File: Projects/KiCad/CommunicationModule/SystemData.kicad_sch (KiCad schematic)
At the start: 23 parts, among them J1 Conn_01x04_Pin, J2 Conn_01x04_Pin, J3 Micro_SD_Card_Det_Hirose_DM3AT, U1 ABX00012, U2 MCP2562-E-P, U3 LT1584-3.3, U4 TLP222A, U5 MCP2515-I/P, Y1 8MHz

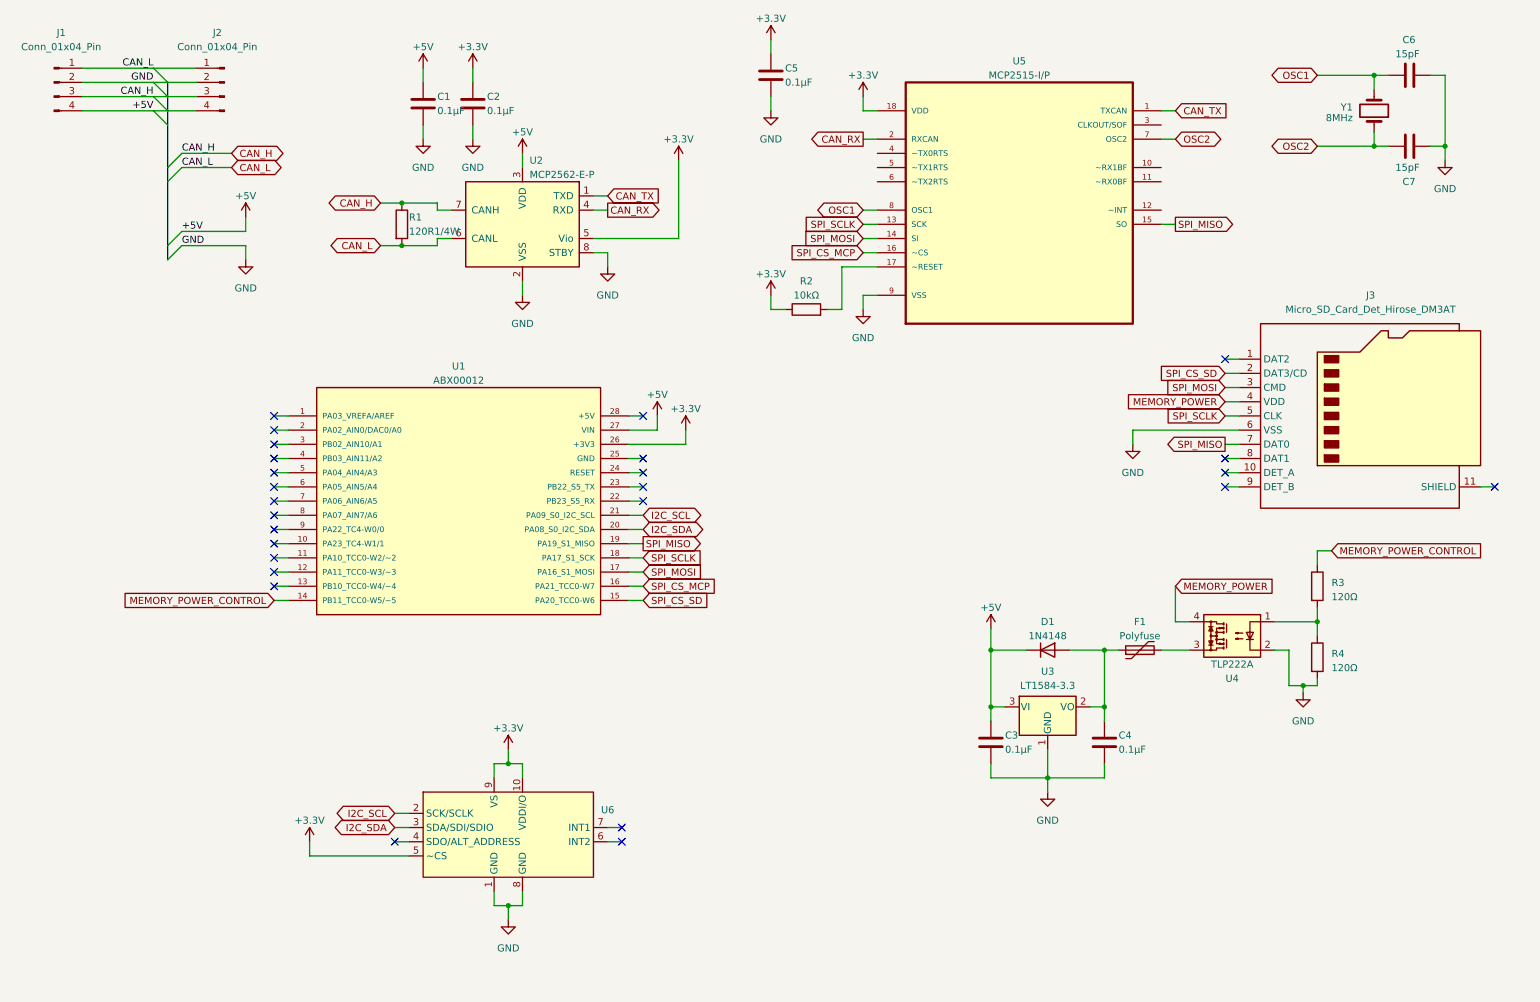
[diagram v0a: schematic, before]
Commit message: ミッションモジュール, エアデータ通信モジュール, システムデータ通信モジュールのKiCadを追加
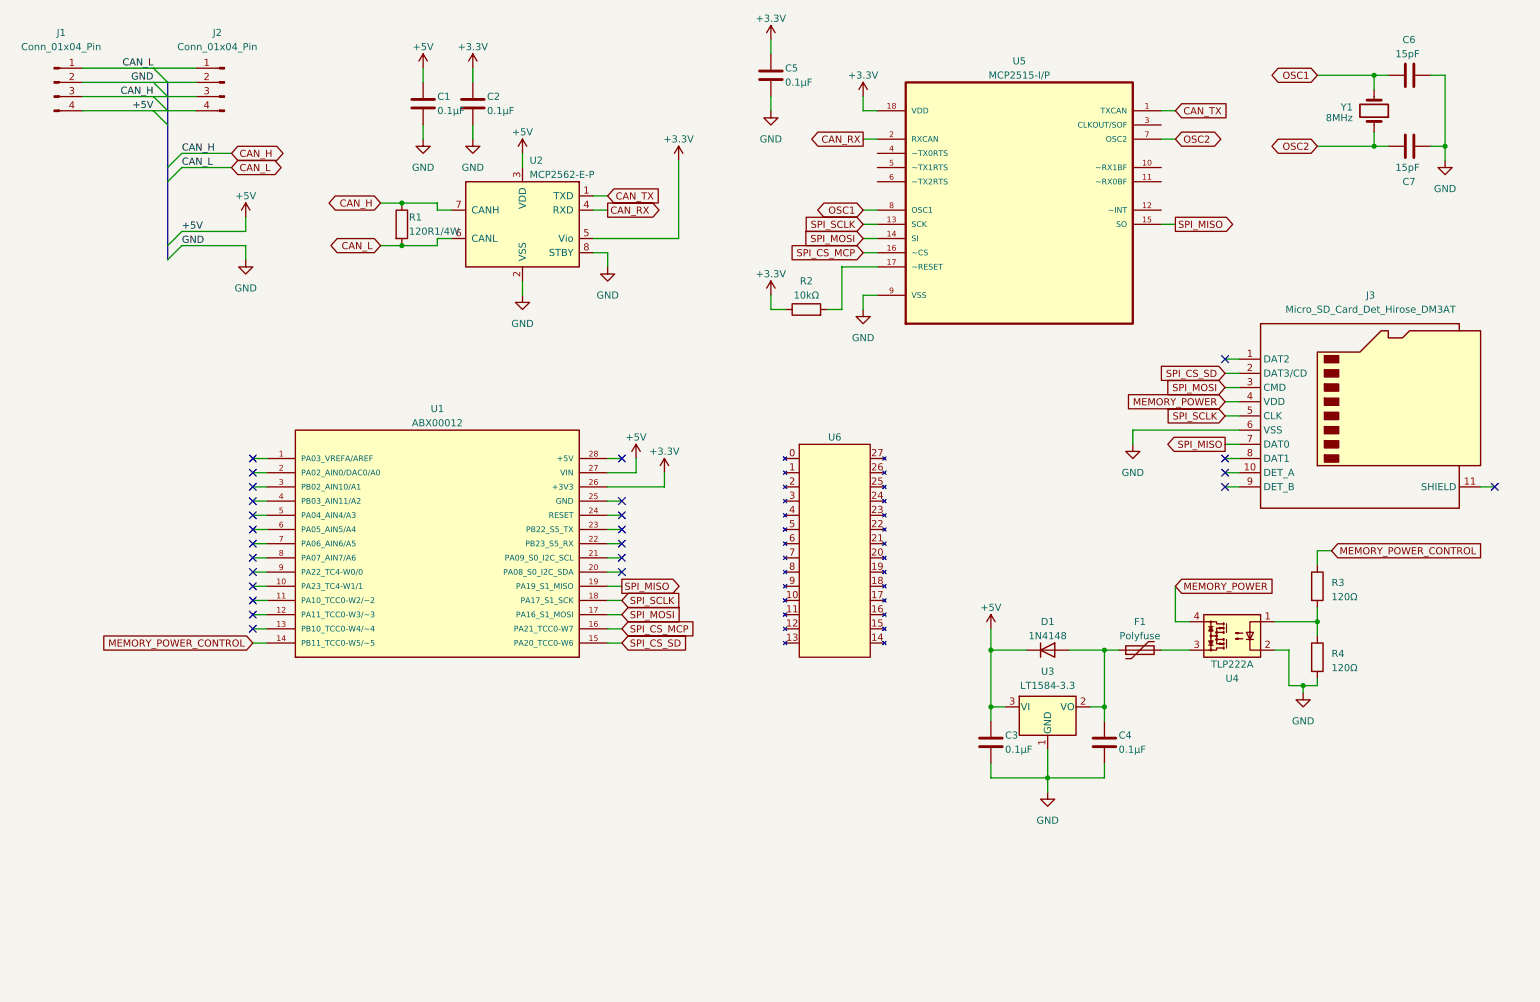
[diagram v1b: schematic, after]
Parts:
- removed U6: ~, StrawberryLinux_ADXL375_Module:ADXL375, symbol StrawberryLinux_ADXL375_Module:ADXL375
- added U6: ~, ArduinoMkrGpsShield:Arduino MKR GPS Shield, symbol ArduinoMkrGpsShield:Arduino_MKR_GPS_Shield
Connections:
- net I2C_SCL: no longer names the net of U1.21 (PA09_S0_I2C_SCL)
- net I2C_SDA: no longer names the net of U1.20 (PA08_S0_I2C_SDA)
- no-connect marks 26 -> 25
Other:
- moved on the sheet: U1

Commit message: 全モジュールのkicadを一通り作った
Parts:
- removed C3, C4: 0.1μF, Capacitor_SMD:C_0805_2012Metric_Pad1.18x1.45mm_HandSolder, symbol Device:C
- removed D1: 1N4148, Diode_THT:D_DO-35_SOD27_P7.62mm_Horizontal, symbol Diode:1N4148
- removed F1: Polyfuse, Fuse:Fuse_BelFuse_0ZRE0005FF_L8.3mm_W3.8mm, symbol Device:Polyfuse
- removed J3: Micro_SD_Card_Det_Hirose_DM3AT, Connector_Card:microSD_HC_Hirose_DM3AT-SF-PEJM5, symbol Connector:Micro_SD_Card_Det_Hirose_DM3AT
- removed U3: LT1584-3.3, Package_TO_SOT_THT:TO-220-3_Vertical, symbol Regulator_Linear:LT1584-3.3
- removed U4: TLP222A, Package_DIP:DIP-4_W7.62mm, symbol Relay_SolidState:TLP222A
- added D1, D2, D3, D4, D5, D6: LED, LED_SMD:LED_1206_3216Metric_Pad1.42x1.75mm_HandSolder, symbol Device:LED
- added R5, R6, R7, R8: 100Ω, Resistor_SMD:R_0805_2012Metric_Pad1.20x1.40mm_HandSolder, symbol Device:R
- added SW1: SW_Push, Button_Switch_THT:SW_PUSH_6mm, symbol Switch:SW_Push
- R2: footprint (none) -> Resistor_SMD:R_0805_2012Metric_Pad1.20x1.40mm_HandSolder
- R3: value 120Ω -> 2kΩ
- R4: value 120Ω -> 100Ω
- renumbered C5 to C3, C6 to C4, C7 to C5, U6 to U3, U5 to U4
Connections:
- net +5V: now also R3.1
- net GND: now also D1.1 (K), D2.1 (K), D3.1 (K), D4.1 (K), D5.1 (K), D6.1 (K), SW1.1; no longer R4.2
- net at R3.2: now also D1.2 (A); no longer R4.1
- net CAN_RECEIVE_STATUS: now reaches U1.10 (PA23_TC4-W1/1)
- net CAN_RECEIVE_STATUS: now also R4.1
- net CAN_SEND_STATUS: now reaches U1.11 (PA10_TCC0-W2/~2)
- net CAN_SEND_STATUS: now also R5.1
- net LORA_RECEIVE_STATUS: now reaches U1.12 (PA11_TCC0-W3/~3)
- net LORA_RECEIVE_STATUS: now also R6.1
- net LORA_SEND_STATUS: now reaches U1.13 (PB10_TCC0-W4/~4)
- net LORA_SEND_STATUS: now also R7.1
- net DEBUG_MODE: now reaches U1.9 (PA22_TC4-W0/0)
- net DEBUG_MODE: now also SW1.2
- net MEMORY_POWER_CONTROL renamed GNSS_STATUS
- net GNSS_STATUS: now also R8.1; no longer R3.1
- net SPI_CS_SD: no longer names the net of U1.15 (PA20_TCC0-W6)
- new net: D6.2 (A), R8.2
- new net: D2.2 (A), R4.2
- new net: D3.2 (A), R5.2
- new net: D5.2 (A), R7.2
- new net: D4.2 (A), R6.2
- no-connect marks 25 -> 16

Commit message: 一通り部品を選定
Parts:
- C4, C5: footprint Capacitor_SMD:C_0805_2012Metric_Pad1.18x1.45mm_HandSolder -> Capacitor_SMD:C_0603_1608Metric_Pad1.08x0.95mm_HandSolder
- D1: value LED -> RED; footprint LED_SMD:LED_1206_3216Metric_Pad1.42x1.75mm_HandSolder -> LED_SMD:LED_0603_1608Metric_Pad1.05x0.95mm_HandSolder
- D2, D3, D4, D5: value LED -> ORANGE; footprint LED_SMD:LED_1206_3216Metric_Pad1.42x1.75mm_HandSolder -> LED_SMD:LED_0603_1608Metric_Pad1.05x0.95mm_HandSolder
- D6: value LED -> GREEN; footprint LED_SMD:LED_1206_3216Metric_Pad1.42x1.75mm_HandSolder -> LED_SMD:LED_0603_1608Metric_Pad1.05x0.95mm_HandSolder
- R1: value 120R1/4W -> 120Ω; footprint Resistor_SMD:R_0805_2012Metric_Pad1.20x1.40mm_HandSolder -> Resistor_SMD:R_0603_1608Metric_Pad0.98x0.95mm_HandSolder
- R2, R4, R5, R6, R7: footprint Resistor_SMD:R_0805_2012Metric_Pad1.20x1.40mm_HandSolder -> Resistor_SMD:R_0603_1608Metric_Pad0.98x0.95mm_HandSolder
- R3: value 2kΩ -> 620Ω; footprint Resistor_SMD:R_0805_2012Metric_Pad1.20x1.40mm_HandSolder -> Resistor_SMD:R_0603_1608Metric_Pad0.98x0.95mm_HandSolder
- R8: value 100Ω -> 300Ω; footprint Resistor_SMD:R_0805_2012Metric_Pad1.20x1.40mm_HandSolder -> Resistor_SMD:R_0603_1608Metric_Pad0.98x0.95mm_HandSolder
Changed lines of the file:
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@@
       (effects (font (size 1.27 1.27)) (justify left))
     )
-    (property "Value" "100Ω" (at 276.86 105.4099 0)
-      (effects (font (size 1.27 1.27)) (justify left))
-    )
-    (property "Footprint" "Resistor_SMD:R_0805_2012Metric_Pad1.20x1.40mm_HandSolder" (at 272.542 104.14 90)
+    (property "Value" "300Ω" (at 276.86 105.4099 0)
+      (effects (font (size 1.27 1.27)) (justify left))
+    )
+    (property "Footprint" "Resistor_SMD:R_0603_1608Metric_Pad0.98x0.95mm_HandSolder" (at 272.542 104.14 90)
       (effects (font (size 1.27 1.27)) hide)
     )
@@
       (effects (font (size 1.27 1.27)))
     )
-    (property "Footprint" "Resistor_SMD:R_0805_2012Metric_Pad1.20x1.40mm_HandSolder" (at 156.21 70.358 90)
+    (property "Footprint" "Resistor_SMD:R_0603_1608Metric_Pad0.98x0.95mm_HandSolder" (at 156.21 70.358 90)
       (effects (font (size 1.27 1.27)) hide)
     )
@@
       (effects (font (size 1.27 1.27)) (justify left))
     )
-    (property "Footprint" "Capacitor_SMD:C_0805_2012Metric_Pad1.18x1.45mm_HandSolder" (at 260.35 38.4048 0)
+    (property "Footprint" "Capacitor_SMD:C_0603_1608Metric_Pad1.08x0.95mm_HandSolder" (at 260.35 38.4048 0)
       (effects (font (size 1.27 1.27)) hide)
     )
@@
       (effects (font (size 1.27 1.27)) (justify left))
     )
-    (property "Value" "2kΩ" (at 227.33 105.4099 0)
-      (effects (font (size 1.27 1.27)) (justify left))
-    )
-    (property "Footprint" "Resistor_SMD:R_0805_2012Metric_Pad1.20x1.40mm_HandSolder" (at 223.012 104.14 90)
+    (property "Value" "620Ω" (at 227.33 105.4099 0)
+      (effects (font (size 1.27 1.27)) (justify left))
+    )
+    (property "Footprint" "Resistor_SMD:R_0603_1608Metric_Pad0.98x0.95mm_HandSolder" (at 223.012 104.14 90)
       (effects (font (size 1.27 1.27)) hide)
     )
@@
       (effects (font (size 1.27 1.27)) (justify right))
     )
-    (property "Value" "LED" (at 228.6 117.1574 90)
-      (effects (font (size 1.27 1.27)) (justify right))
-    )
-    (property "Footprint" "LED_SMD:LED_1206_3216Metric_Pad1.42x1.75mm_HandSolder" (at 224.79 114.3 0)
+    (property "Value" "RED" (at 228.6 117.1574 90)
+      (effects (font (size 1.27 1.27)) (justify right))
+    )
+    (property "Footprint" "LED_SMD:LED_0603_1608Metric_Pad1.05x0.95mm_HandSolder" (at 224.79 114.3 0)
       (effects (font (size 1.27 1.27)) hide)
     )
@@
       (effects (font (size 1.27 1.27)) (justify left))
     )
-    (property "Footprint" "Resistor_SMD:R_0805_2012Metric_Pad1.20x1.40mm_HandSolder" (at 231.902 104.14 90)
+    (property "Footprint" "Resistor_SMD:R_0603_1608Metric_Pad0.98x0.95mm_HandSolder" (at 231.902 104.14 90)
       (effects (font (size 1.27 1.27)) hide)
     )
@@
       (effects (font (size 1.27 1.27)) (justify right))
     )
-    (property "Value" "LED" (at 247.65 117.1574 90)
-      (effects (font (size 1.27 1.27)) (justify right))
-    )
-    (property "Footprint" "LED_SMD:LED_1206_3216Metric_Pad1.42x1.75mm_HandSolder" (at 243.84 114.3 0)
+    (property "Value" "ORANGE" (at 247.65 117.1574 90)
+      (effects (font (size 1.27 1.27)) (justify right))
+    )
+    (property "Footprint" "LED_SMD:LED_0603_1608Metric_Pad1.05x0.95mm_HandSolder" (at 243.84 114.3 0)
       (effects (font (size 1.27 1.27)) hide)
     )
@@
       (effects (font (size 1.27 1.27)) (justify right))
     )
-    (property "Value" "LED" (at 267.97 117.1574 90)
-      (effects (font (size 1.27 1.27)) (justify right))
-    )
-    (property "Footprint" "LED_SMD:LED_1206_3216Metric_Pad1.42x1.75mm_HandSolder" (at 264.16 114.3 0)
+    (property "Value" "ORANGE" (at 267.97 117.1574 90)
+      (effects (font (size 1.27 1.27)) (justify right))
+    )
+    (property "Footprint" "LED_SMD:LED_0603_1608Metric_Pad1.05x0.95mm_HandSolder" (at 264.16 114.3 0)
       (effects (font (size 1.27 1.27)) hide)
     )
@@
       (effects (font (size 1.27 1.27)) (justify left))
     )
-    (property "Footprint" "Resistor_SMD:R_0805_2012Metric_Pad1.20x1.40mm_HandSolder" (at 242.062 104.14 90)
+    (property "Footprint" "Resistor_SMD:R_0603_1608Metric_Pad0.98x0.95mm_HandSolder" (at 242.062 104.14 90)
       (effects (font (size 1.27 1.27)) hide)
     )
@@
       (effects (font (size 1.27 1.27)) (justify right))
     )
-    (property "Value" "LED" (at 278.13 117.1574 90)
-      (effects (font (size 1.27 1.27)) (justify right))
-    )
-    (property "Footprint" "LED_SMD:LED_1206_3216Metric_Pad1.42x1.75mm_HandSolder" (at 274.32 114.3 0)
+    (property "Value" "GREEN" (at 278.13 117.1574 90)
+      (effects (font (size 1.27 1.27)) (justify right))
+    )
+    (property "Footprint" "LED_SMD:LED_0603_1608Metric_Pad1.05x0.95mm_HandSolder" (at 274.32 114.3 0)
       (effects (font (size 1.27 1.27)) hide)
     )
@@
       (effects (font (size 1.27 1.27)) (justify right))
     )
-    (property "Value" "LED" (at 237.49 117.1574 90)
-      (effects (font (size 1.27 1.27)) (justify right))
-    )
-    (property "Footprint" "LED_SMD:LED_1206_3216Metric_Pad1.42x1.75mm_HandSolder" (at 233.68 114.3 0)
+    (property "Value" "ORANGE" (at 237.49 117.1574 90)
+      (effects (font (size 1.27 1.27)) (justify right))
+    )
+    (property "Footprint" "LED_SMD:LED_0603_1608Metric_Pad1.05x0.95mm_HandSolder" (at 233.68 114.3 0)
       (effects (font (size 1.27 1.27)) hide)
     )
@@
       (effects (font (size 1.27 1.27)) (justify left))
     )
-    (property "Footprint" "Capacitor_SMD:C_0805_2012Metric_Pad1.18x1.45mm_HandSolder" (at 260.35 25.7048 0)
+    (property "Footprint" "Capacitor_SMD:C_0603_1608Metric_Pad1.08x0.95mm_HandSolder" (at 260.35 25.7048 0)
       (effects (font (size 1.27 1.27)) hide)
     )
@@
       (effects (font (size 1.27 1.27)) (justify left))
     )
-    (property "Footprint" "Resistor_SMD:R_0805_2012Metric_Pad1.20x1.40mm_HandSolder" (at 252.222 104.14 90)
+    (property "Footprint" "Resistor_SMD:R_0603_1608Metric_Pad0.98x0.95mm_HandSolder" (at 252.222 104.14 90)
       (effects (font (size 1.27 1.27)) hide)
     )
@@
       (effects (font (size 1.27 1.27)) (justify right))
     )
-    (property "Value" "LED" (at 257.81 117.1574 90)
-      (effects (font (size 1.27 1.27)) (justify right))
-    )
-    (property "Footprint" "LED_SMD:LED_1206_3216Metric_Pad1.42x1.75mm_HandSolder" (at 254 114.3 0)
+    (property "Value" "ORANGE" (at 257.81 117.1574 90)
+      (effects (font (size 1.27 1.27)) (justify right))
+    )
+    (property "Footprint" "LED_SMD:LED_0603_1608Metric_Pad1.05x0.95mm_HandSolder" (at 254 114.3 0)
       (effects (font (size 1.27 1.27)) hide)
     )
@@
       (effects (font (size 1.27 1.27)) (justify left))
     )
-    (property "Footprint" "Resistor_SMD:R_0805_2012Metric_Pad1.20x1.40mm_HandSolder" (at 262.382 104.14 90)
+    (property "Footprint" "Resistor_SMD:R_0603_1608Metric_Pad0.98x0.95mm_HandSolder" (at 262.382 104.14 90)
       (effects (font (size 1.27 1.27)) hide)
     )
@@
       (effects (font (size 1.27 1.27)) (justify left))
     )
-    (property "Value" "120R1/4W" (at 85.09 54.61 0)
-      (effects (font (size 1.27 1.27)) (justify left))
-    )
-    (property "Footprint" "Resistor_SMD:R_0805_2012Metric_Pad1.20x1.40mm_HandSolder" (at 82.042 53.34 90)
-      (effects (font (size 1.27 1.27)) hide)
-    )
+    (property "Value" "120Ω" (at 85.09 54.61 0)
+      (effects (font (size 1.27 1.27)) (justify left))
+    )
+    (property "Footprint" "Resistor_SMD:R_0603_1608Metric_Pad0.98x0.95mm_HandSolder" (at 82.042 53.34 90)
+      (effects (font (size 1.27 1.27)) hide)
+    )

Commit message: コネクタを再配置, 基板上で12V->5Vをするように変更
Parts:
- removed J1, J2: Conn_01x04_Pin, Connector_JST:JST_XH_S4B-XH-A_1x04_P2.50mm_Horizontal, symbol Connector:Conn_01x04_Pin
- added C6: 0.33μF, Capacitor_SMD:C_0805_2012Metric_Pad1.18x1.45mm_HandSolder, symbol Device:C
- added C7: 0.1μF, Capacitor_SMD:C_0805_2012Metric_Pad1.18x1.45mm_HandSolder, symbol Device:C
- added C8: 100μF, Capacitor_SMD:CP_Elec_6.3x7.7, symbol Device:C_Polarized
- added D7: 1N4007, Diode_SMD:D_SOD-123F, symbol Diode:1N4007
- added J3: Conn_01x08, Connector_Hirose:Hirose_DF11-8DP-2DSA_2x04_P2.00mm_Vertical, symbol Connector_Generic:Conn_01x08
- added U5: NJM7805SDL1, Package_TO_SOT_SMD:TO-252-3_TabPin2, symbol Regulator_Linear:L7805
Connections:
- net +5V: now also C7.1, C8.1, D7.2 (A), U5.3 (OUT)
- net CAN_H: now also J3.7 (Pin_7), J3.8 (Pin_8)
- net CAN_L: now also J3.3 (Pin_3), J3.4 (Pin_4)
- net GND: now also C6.2, C7.2, C8.2, J3.5 (Pin_5), J3.6 (Pin_6), U5.2 (GND)
- new net +12V: C6.1, D7.1 (K), J3.1 (Pin_1), J3.2 (Pin_2), U5.1 (IN)
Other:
- moved on the sheet: D1, D2, D3, D4, D5, D6, R3, R4, R5, R6, R7, R8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

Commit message: 基板設計の都市伝説をいろいろ適応
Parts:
- U4: renamed from U1; footprint ARDUINO_ABX00012 -> ABX00012:ARDUINO_ABX00012
- renumbered C4 to C1, C3 to C2, C6 to C3, C2 to C4, C1 to C5, C8 to C6, C5 to C8, D7 to D2, D2 to D4, D4 to D5, D5 to D6, D6 to D7, J3 to J1, R3 to R2, R2 to R3, R5 to R4, R4 to R5, U2 to U1, U4 to U2, U5 to U3, U3 to U5

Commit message: テストポイントを追加
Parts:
- added TP1, TP2: TestPoint, Connector_Pin:Pin_D1.0mm_L10.0mm, symbol Connector:TestPoint
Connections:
- net CAN_H: now also TP1.1
- net CAN_L: now also TP2.1
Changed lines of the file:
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@@
+    )
+  )
+  (symbol (lib_id "Connector:TestPoint") (at 83.82 57.15 180) (unit 1)
+    (in_bom yes) (on_board yes) (dnp no) (fields_autoplaced)
+    (property "Reference" "TP2" (at 86.36 59.817 0)
+      (effects (font (size 1.27 1.27)) (justify right))
+    )
+    (property "Value" "TestPoint" (at 86.36 62.357 0)
+      (effects (font (size 1.27 1.27)) (justify right))
+    )
+    (property "Footprint" "Connector_Pin:Pin_D1.0mm_L10.0mm" (at 78.74 57.15 0)
+      (effects (font (size 1.27 1.27)) hide)
+    )
+    (property "Datasheet" "~" (at 78.74 57.15 0)
+      (effects (font (size 1.27 1.27)) hide)
+    )
+    (pin "1")
+    (instances
+      (project "SystemData"
+        (path "/ea1ed597-7cd3-4340-902e-bdce8f2d7a62"
+          (reference "TP2") (unit 1)
+        )
+      )
     )
   )
@@
         )
       )
+    )
+  )
+  (symbol (lib_id "Connector:TestPoint") (at 83.82 49.53 0) (unit 1)
+    (in_bom yes) (on_board yes) (dnp no) (fields_autoplaced)
+    (property "Reference" "TP1" (at 86.36 45.593 0)
+      (effects (font (size 1.27 1.27)) (justify left))
+    )
+    (property "Value" "TestPoint" (at 86.36 48.133 0)
+      (effects (font (size 1.27 1.27)) (justify left))
+    )
+    (property "Footprint" "Connector_Pin:Pin_D1.0mm_L10.0mm" (at 88.9 49.53 0)
+      (effects (font (size 1.27 1.27)) hide)
+    )
+    (property "Datasheet" "~" (at 88.9 49.53 0)
+      (effects (font (size 1.27 1.27)) hide)
+    )
+    (pin "1")
+    (instances
+      (project "SystemData"
+        (path "/ea1ed597-7cd3-4340-902e-bdce8f2d7a62"
+          (reference "TP1") (unit 1)
+        )
+      )
